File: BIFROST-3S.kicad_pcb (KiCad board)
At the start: 2 copper layers, 60 x 40 mm, 6 parts, among them J1 1-776267-1, J2 200241-1222, J3 200241-1222, J4 B6B-XH-A_LF__SN_, J5 B4B-XH-A_LF__SN_

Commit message: Schematic+Layout 2.0
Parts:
- removed J1: 1-776267-1, 1-776267-1:17762671
- added J6: 560020-1020, 560020-1020:5600201020, F.Cu at (131.4, 112.3)
- added J7: 200241-1222, 200241-1222:2002411222, F.Cu at (123.9, 94.3)
- moved J5 5.56 mm to (171.0, 113.7), turned to 90 degrees
- moved J3 4.58 mm to (160.0, 94.3)
- moved J2 4.52 mm to (142.0, 94.3)
- moved D1 3.11 mm to (163.8, 98.6)
- moved J4 2.58 mm to (150.6, 114.6), turned to 0 degrees
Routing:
- net /BQ2_TS1: track 32.0 -> 51.8 mm
- net /BAT1: track 31.6 -> 19.0 mm
- net /BQ2_TS2: track 39.3 -> 50.4 mm
- net /BQ2_TS3: track 38.6 -> 49.1 mm
- net /BQ_TS: track 24.7 -> 33.7 mm
- net /BAT2: track 31.4 -> 24.0 mm
- net /BAT3: track 30.6 -> 28.8 mm

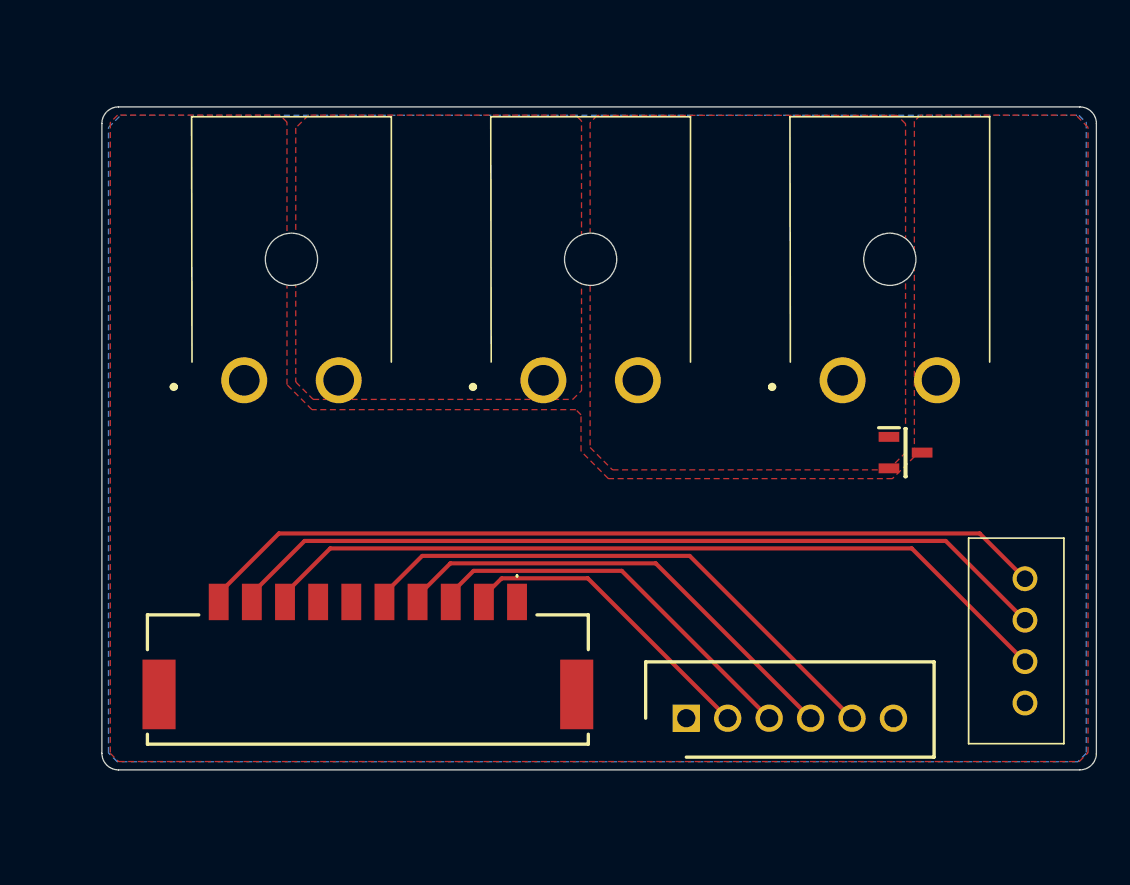
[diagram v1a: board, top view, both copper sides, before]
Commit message: Fixed Polygons and Silkscreen
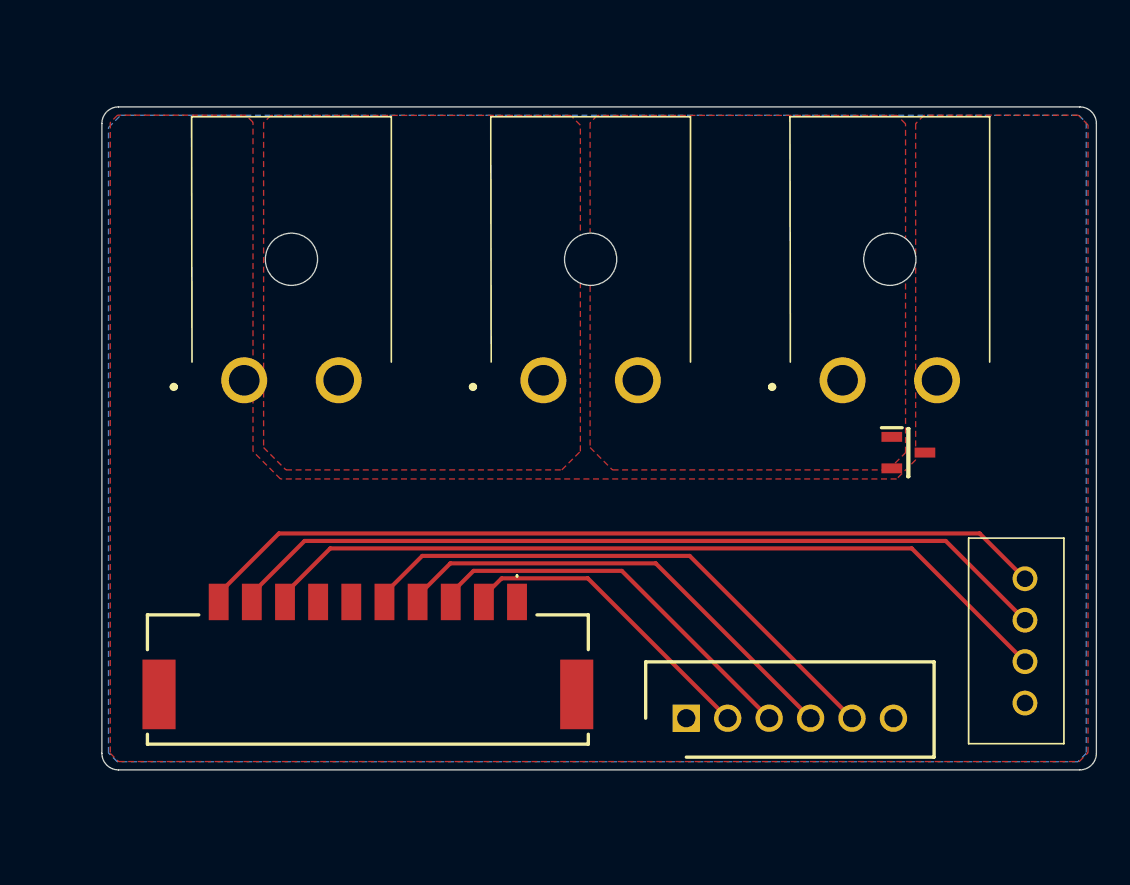
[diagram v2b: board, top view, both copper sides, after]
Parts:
- added G***: LOGO, LOGO, B.Cu at (145.4, 97.7)
- moved D1 0.17 mm to (164.0, 98.6)

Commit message: Schematic+Layout 3.0
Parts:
- removed J2: 200241-1222, 200241-1222:2002411222
- added F1: MF-RHS800-0, MF-RHS800-0:MFRHS8000, F.Cu at (147.2, 100.1)
- moved J5 34.4 mm to (137.1, 119.0), turned to 0 degrees
- moved J4 33.1 mm to (117.8, 119.0)
- moved J7 28.7 mm to (152.6, 93.3), turned to 90 degrees
- moved D1 21.8 mm to (147.1, 112.4), turned to -90 degrees
- moved J6 21.1 mm to (129.0, 91.4), turned to 180 degrees
- moved J3 17.0 mm to (152.6, 109.6), turned to 90 degrees
- moved G*** 7.90 mm to (141.7, 104.7)
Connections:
- net /BAT3 renamed /BAT3/PACK+
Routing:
- net /BQ2_TS1: track 51.8 -> 25.7 mm
- net /BQ2_TS2: track 50.4 -> 25.5 mm
- net /BQ2_TS3: track 49.1 -> 25.3 mm
- net /BQ_TS: track 33.7 -> 23.0 mm
- net /BAT3/PACK+: track 28.8 -> 23.2 mm
- net /BAT1: track 19.0 -> 23.6 mm
- net /BAT2: track 24.0 -> 23.4 mm
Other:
- board size 60 x 40 mm -> 54 x 36 mm

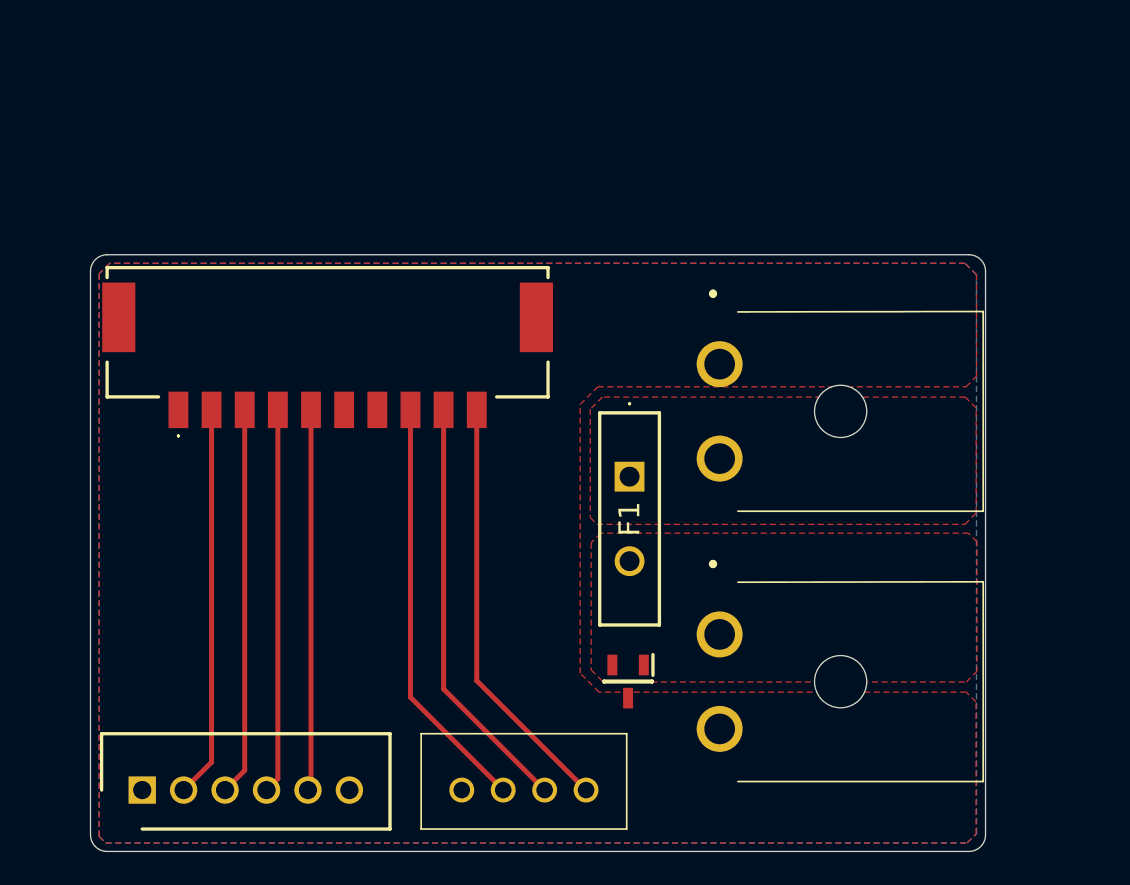
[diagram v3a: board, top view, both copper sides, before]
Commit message: Finalized Silkscreen
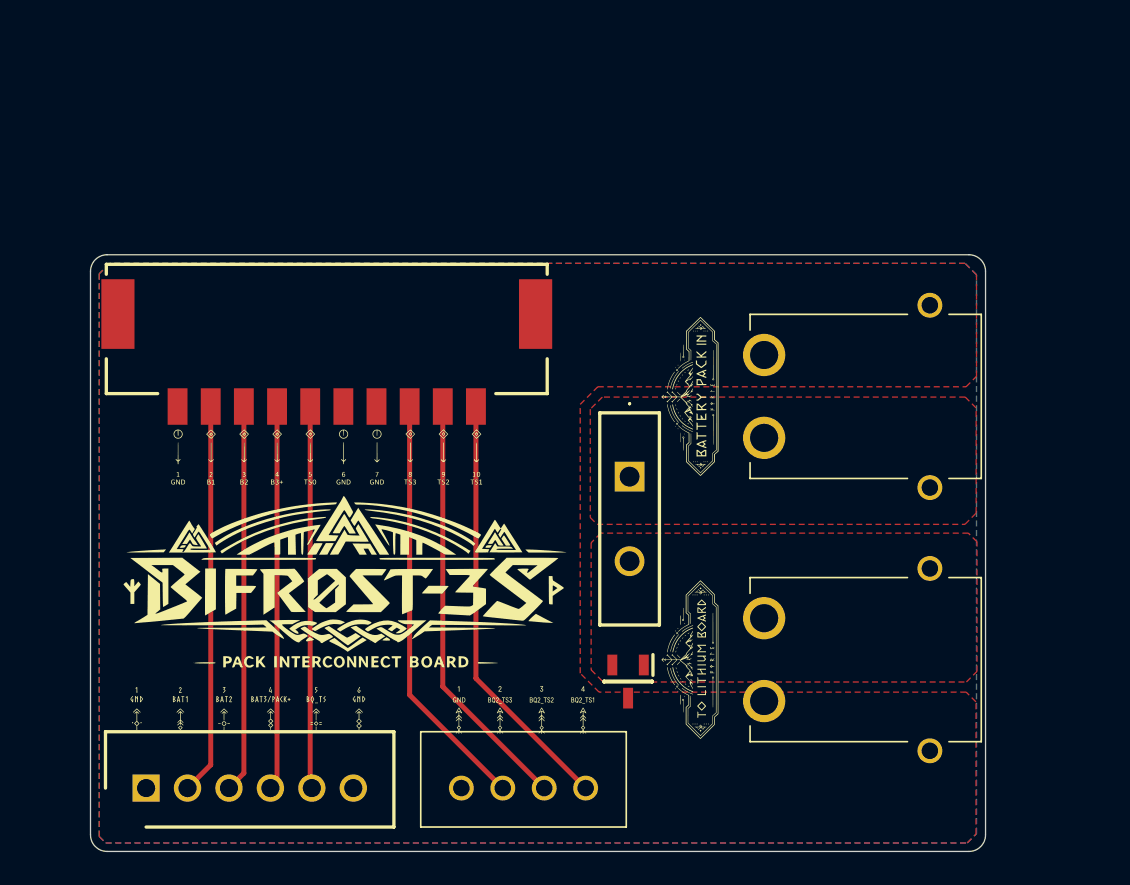
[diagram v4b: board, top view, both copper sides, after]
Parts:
- removed J6: 560020-1020, 560020-1020:5600201020
- removed J7: 200241-1222, 200241-1222:2002411222
- added G***: LOGO, LOGO, F.Cu at (151.2, 95.2)
- added G***: LOGO, LOGO, F.Cu at (129.1, 98.8)
- added G***: LOGO, LOGO, F.Cu at (130.2, 108.0)
- added G***: LOGO, LOGO, F.Cu at (124.2, 114.0)
- added G***: LOGO, LOGO, F.Cu at (140.6, 114.2)
- added G***: LOGO, LOGO, F.Cu at (150.9, 111.1)
- added J1: B6B-XH-A_LF__SN_, B6B-XH-A_LF__SN_:SHDR6W64P0X250_1X6_1740X575X700P, F.Cu at (118.0, 118.9)
- added J2: 560020-1020, 560020-1020:5600201020, F.Cu at (128.9, 91.2)
- J3: value 200241-1222 -> B4B-XH-A_LF__SN_; footprint 200241-1222:2002411222 -> B4B-XH-A_LF__SN_:B4BXHALFSN
- J4: value B6B-XH-A_LF__SN_ -> XT30PW-M; footprint B6B-XH-A_LF__SN_:SHDR6W64P0X250_1X6_1740X575X700P -> XT30PW-M:XT30PWM
- J5: value B4B-XH-A_LF__SN_ -> XT30PW-M; footprint B4B-XH-A_LF__SN_:B4BXHALFSN -> XT30PW-M:XT30PWM
- moved J4 44.1 mm to (161.2, 111.1), turned to -90 degrees
- moved J5 33.9 mm to (161.2, 95.2), turned to -90 degrees
- moved J3 18.1 mm to (137.0, 118.9), turned to 0 degrees
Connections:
- J3 pad 1: /+BATT -> GND
- J3 pad 2: GND -> /BQ2_TS3
- J4 pad 1: GND -> /+BATT
- J4 pad 2: /BAT1 -> GND
- J4 pad 3: /BAT2 -> unconnected-(J4-Pad3)
- J4 pad 4: /BAT3/PACK+ -> unconnected-(J4-Pad4)
- J5 pad 2: /BQ2_TS3 -> /PACK+_RAW
- J5 pad 3: /BQ2_TS2 -> unconnected-(J5-Pad3)
- J5 pad 4: /BQ2_TS1 -> unconnected-(J5-Pad4)

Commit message: Layout 3.1
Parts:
- moved F1 14.8 mm to (161.2, 104.8), turned to 180 degrees
- moved D1 10.7 mm to (149.7, 102.1), turned to 180 degrees
- moved J4 4.75 mm to (158.8, 115.2), turned to 180 degrees
- moved G*** 3.05 mm to (150.1, 114.1)
- moved J5 2.37 mm to (159.0, 94.3), turned to 0 degrees
- moved G*** 1.06 mm to (150.4, 94.5)
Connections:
- J4 pad 1: /+BATT -> GND
- J4 pad 2: GND -> /+BATT

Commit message: Gerbers+Step
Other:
- board text added: "+"
- board text added: "-"
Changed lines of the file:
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@@
 		(tags "TVS Diode (Bi-directional)")
 		(property "Reference" "D1"
-			(at 2.4975 -3.74 0)
+			(at 0.02 1.974651 0)
 			(layer "B.SilkS")
 			(effects
@@
 		)
 		(fp_text user "${REFERENCE}"
-			(at 2.4975 -3.74 0)
+			(at 0.02 1.98 0)
 			(layer "B.Fab")
 			(effects
@@
 		(layer "Edge.Cuts")
 	)
+	(gr_text "-"
+		(at 151.79 101.1 0)
+		(layer "F.SilkS")
+		(effects
+			(font
+				(size 1.5 1.5)
+				(thickness 0.3)
+				(bold yes)
+			)
+			(justify left bottom)
+		)
+	)
+	(gr_text "+"
+		(at 151.521742 110.801639 0)
+		(layer "F.SilkS")
+		(effects
+			(font
+				(size 1.5 1.5)
+				(thickness 0.3)
+				(bold yes)
+			)
+			(justify left bottom)
+		)
+	)
+	(gr_text "+"
+		(at 163.96625 101.1 0)
+		(layer "F.SilkS")
+		(effects
+			(font
+				(size 1.5 1.5)
+				(thickness 0.3)
+				(bold yes)
+			)
+			(justify left bottom)
+		)
+	)
+	(gr_text "-"
+		(at 163.81 110.801639 0)
+		(layer "F.SilkS")
+		(effects
+			(font
+				(size 1.5 1.5)
+				(thickness 0.3)
+				(bold yes)
+			)
+			(justify left bottom)
+		)
+	)
 	(segment

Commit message: Layout 4.0
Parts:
- removed the G*** at (150.4, 94.5)
- removed the G*** at (130.2, 108.0)
- removed the G*** at (150.1, 114.1)
- removed the G*** at (141.7, 104.7)
- added G***: LOGO, LOGO, F.Cu at (155.3, 95.9)
- added G***: LOGO, LOGO, F.Cu at (134.4, 107.1)
- added G***: LOGO, LOGO, F.Cu at (155.2, 111.9)
- added G***: LOGO, LOGO, B.Cu at (145.8, 104.3)
- moved G*** 10.4 mm to (139.4, 100.1)
- moved J2 10.3 mm to (139.1, 92.3)
- moved F1 9.63 mm to (151.8, 102.6), turned to -90 degrees
- moved J1 7.66 mm to (125.5, 117.5)
- moved G*** 7.52 mm to (131.6, 112.8)
- moved G*** 6.94 mm to (147.5, 113.3)
- moved J3 6.78 mm to (143.7, 117.5)
- moved D1 5.12 mm to (147.6, 106.7)
- moved J4 3.88 mm to (161.3, 112.3)
- moved J5 2.68 mm to (161.3, 95.7)
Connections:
- J4 pad 1: GND -> /+BATT
- J4 pad 2: /+BATT -> GND
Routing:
- net /BQ2_TS3: track 25.3 -> 22.2 mm
- net /BQ2_TS2: track 25.6 -> 23.6 mm
- net /BQ_TS: track 23.1 -> 21.6 mm
- net /BAT3/PACK+: track 23.2 -> 21.8 mm
- net /BAT2: track 23.4 -> 22.0 mm
- net /BAT1: track 23.6 -> 22.2 mm
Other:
- board size 54 x 36 mm -> 46 x 34 mm
